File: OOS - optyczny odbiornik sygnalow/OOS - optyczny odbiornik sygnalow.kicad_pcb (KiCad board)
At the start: 2 copper layers, 72 x 79.5 mm, 124 parts, among them J1 Conn_01x02_Pin, J4 Conn_01x02_Socket, J5 Conn_Coaxial, J6 USB_C_Receptacle, Q1 SI2301CDS-T1-GE3, Q2 AOSS32334C, Q3 AOSS32334C, SW1 SW_Rotary_1x8_MP, U1 OPA300AIDBVR, U2 OPA300AIDBVR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

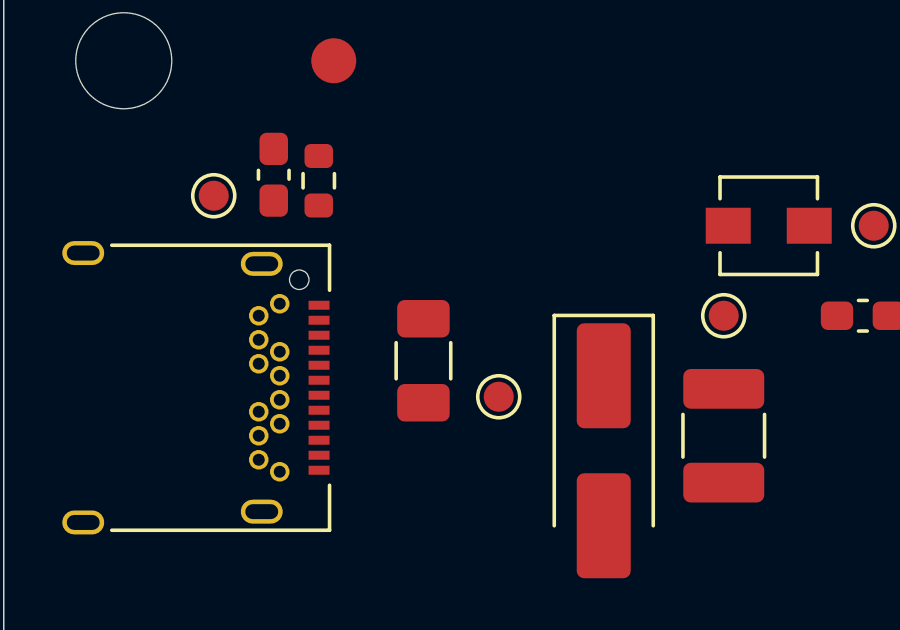
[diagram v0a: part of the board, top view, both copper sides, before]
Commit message: Move testpoint TP37
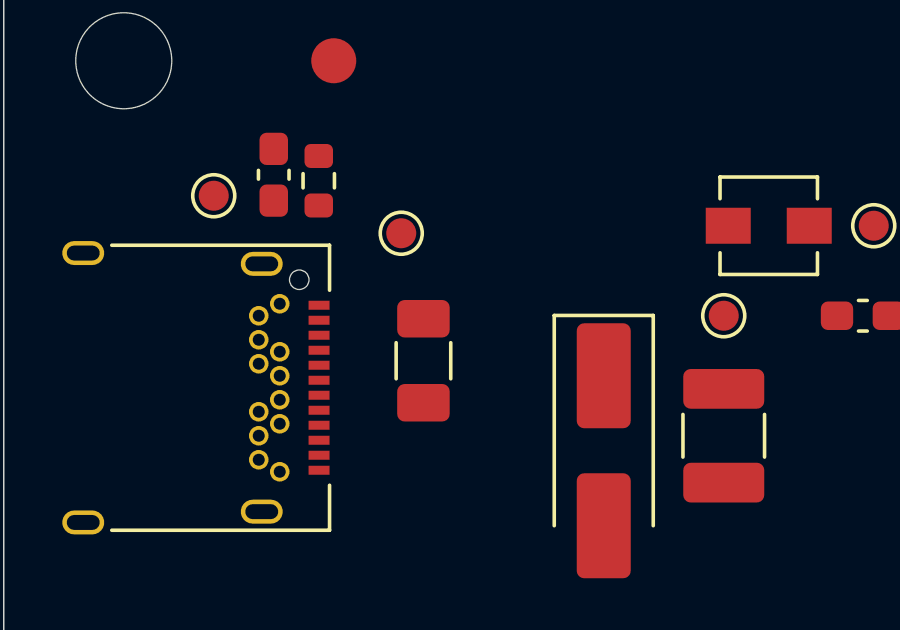
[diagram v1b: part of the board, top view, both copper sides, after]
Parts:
- moved TP37 6.35 mm to (211.7, 38.1)
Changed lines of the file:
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@@
 	(footprint "TestPoint:TestPoint_Pad_D1.0mm"
 		(layer "F.Cu")
-		(at 214.92 43.58 180)
+		(at 211.67 38.13 180)
 		(descr "SMD pad as test Point, diameter 1.0mm")
 		(tags "test point SMD pad")

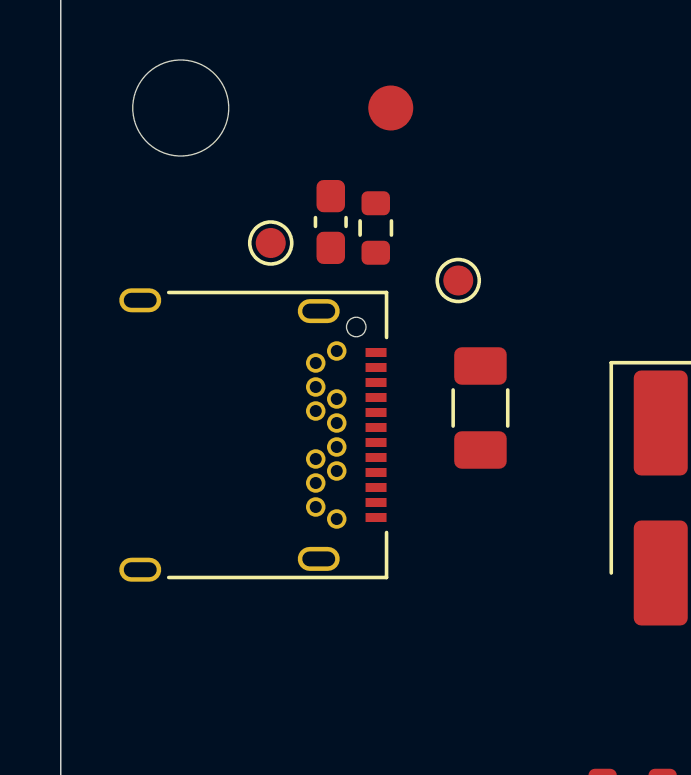
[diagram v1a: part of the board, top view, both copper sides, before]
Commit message: Added polygon for USB3.2, move TP37 on a schematic
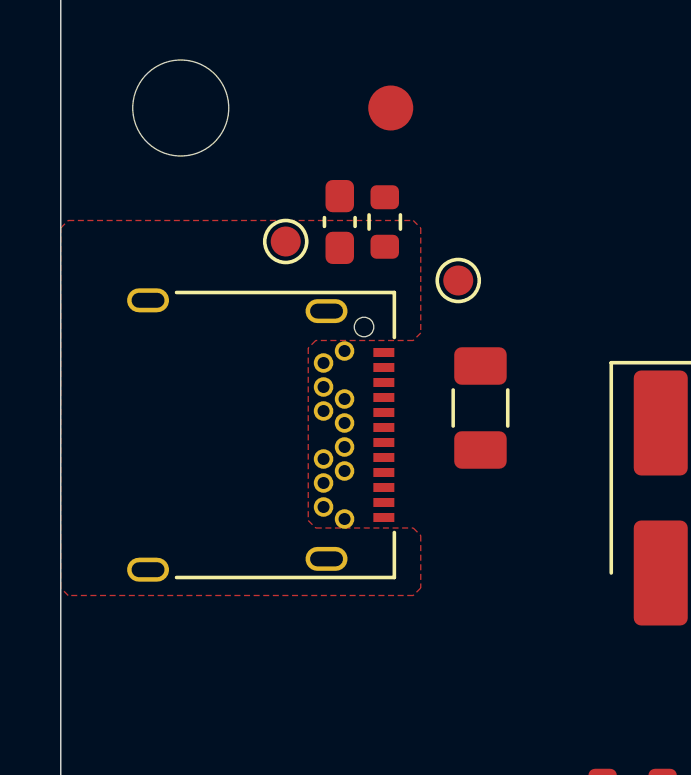
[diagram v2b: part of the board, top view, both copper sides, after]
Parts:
- moved TP38 0.50 mm to (205.9, 36.8)
- moved R26 0.36 mm to (209.2, 36.2)
- moved C25 0.30 mm to (207.7, 36.2)
- moved J6 0.26 mm to (204.2, 43.3)
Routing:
- added copper zone on F.Cu, net Net-(J6-SHIELD)
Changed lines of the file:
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@@
 	(footprint "Connector_USB:USB_C_Receptacle_Amphenol_12401548E4-2A"
 		(layer "F.Cu")
-		(at 203.91 43.28 -90)
+		(at 204.17 43.28 -90)
 		(descr "USB TYPE C, RA RCPT PCB, Hybrid, https://www.amphenolcanada.com/StockAvailabilityPrice.aspx?From=&PartNum=12401548E4%7e2A")
 		(tags "USB C Type-C Receptacle Hybrid")
@@
 	(footprint "Resistor_SMD:R_0603_1608Metric"
 		(layer "F.Cu")
-		(at 208.92 36.38 90)
+		(at 209.22 36.18 90)
 		(descr "Resistor SMD 0603 (1608 Metric), square (rectangular) end terminal, IPC-7351 nominal, (Body size source: IPC-SM-782 page 72, https://www.pcb-3d.com/wordpress/wp-content/uploads/ipc-sm-782a_amendment_1_and_2.pdf), generated with kicad-footprint-generator")
 		(tags "resistor")
@@
 	(footprint "Capacitor_SMD:C_0603_1608Metric_Pad1.08x0.95mm_HandSolder"
 		(layer "F.Cu")
-		(at 207.42 36.18 90)
+		(at 207.72 36.18 90)
 		(descr "Capacitor SMD 0603 (1608 Metric), square (rectangular) end terminal, IPC-7351 nominal with elongated pad for handsoldering. (Body size source: IPC-SM-782 page 76, https://www.pcb-3d.com/wordpress/wp-content/uploads/ipc-sm-782a_amendment_1_and_2.pdf), generated with kicad-footprint-generator")
 		(tags "capacitor handsolder")
@@
 	(footprint "TestPoint:TestPoint_Pad_D1.0mm"
 		(layer "F.Cu")
-		(at 205.42 36.88)
+		(at 205.92 36.83)
 		(descr "SMD pad as test Point, diameter 1.0mm")
 		(tags "test point SMD pad")
@@
 		(net 56)
 	)
+	(zone
+		(net 19)
+		(net_name "Net-(J6-SHIELD)")
+		(layer "F.Cu")
+		(name "Shield")
+		(hatch edge 0.5)
+		(connect_pads
+			(clearance 0.5)
+		)
+		(min_thickness 0.25)
+		(filled_areas_thickness no)
+		(fill yes
+			(thermal_gap 0.2)
+			(thermal_bridge_width 0.4)
+		)
+		(polygon
+			(pts
+				(xy 210.17 36.13) (xy 210.42 36.38) (xy 210.42 39.88) (xy 210.17 40.13) (xy 206.92 40.13) (xy 206.67 40.38)
+				(xy 206.67 46.13) (xy 206.92 46.38) (xy 210.17 46.38) (xy 210.42 46.63) (xy 210.42 48.38) (xy 210.17 48.63)
+				(xy 198.67 48.63) (xy 198.42 48.38) (xy 198.42 36.38) (xy 198.67 36.13)
+			)
+		)
+	)
 	(embedded_fonts no)

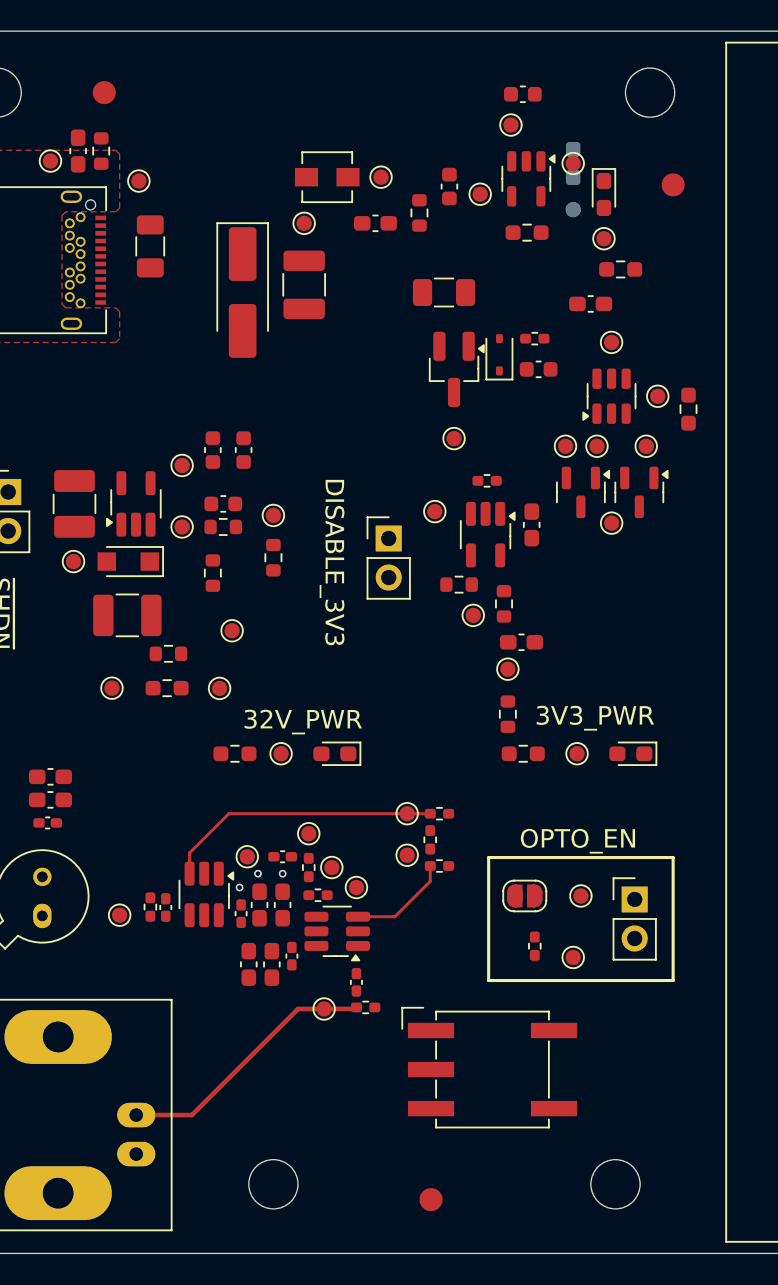
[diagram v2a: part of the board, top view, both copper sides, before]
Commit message: Moved TP37 on schematic, Added LED diode with resistor for +5V indication, improved component placement for USB3.2
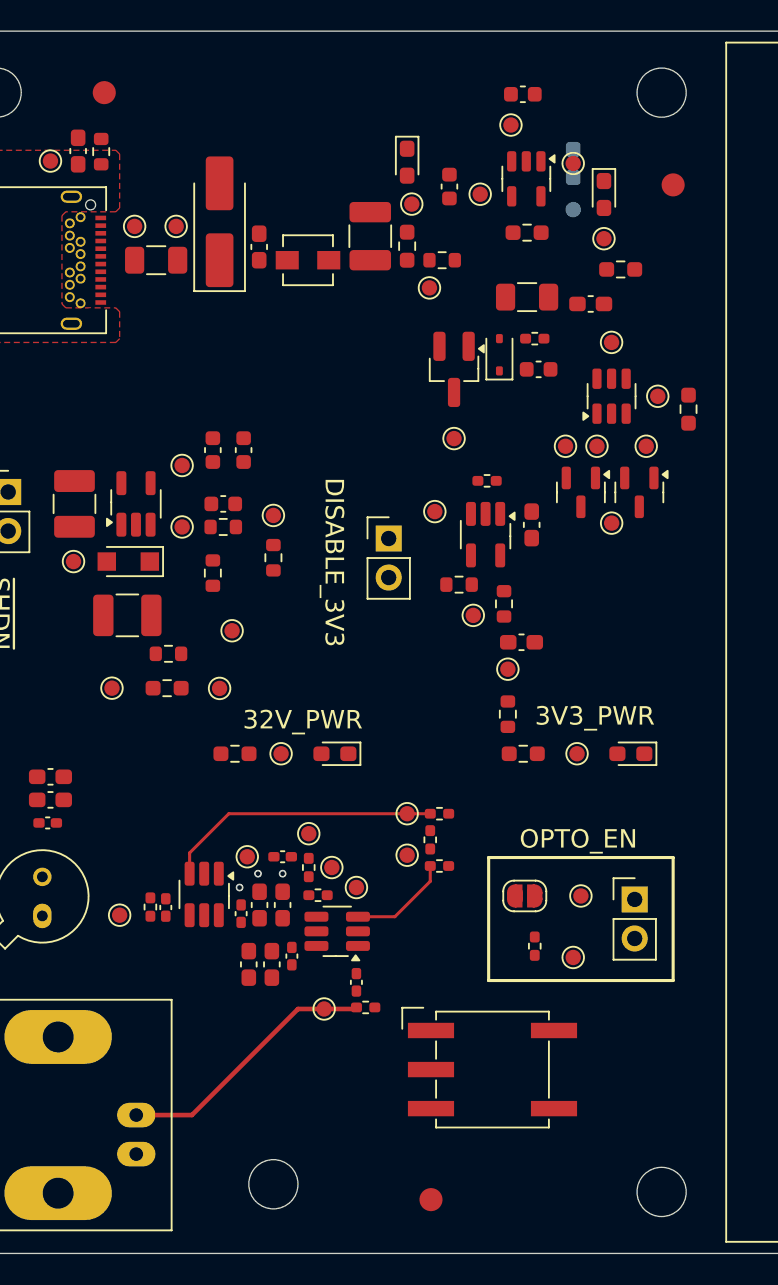
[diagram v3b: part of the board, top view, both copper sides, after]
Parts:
- added D8: LED, Diode_SMD:D_0603_1608Metric_Pad1.05x0.95mm_HandSolder, F.Cu at (229.1, 36.9)
- added R27: 2k2, Resistor_SMD:R_0603_1608Metric_Pad0.98x0.95mm_HandSolder, F.Cu at (229.1, 42.4)
- added TP39: TestPoint_Small, TestPoint:TestPoint_Pad_D1.0mm, F.Cu at (229.4, 39.6)
- moved TP35 8.33 mm to (214.1, 41.1)
- moved TP36 7.86 mm to (230.6, 45.1)
- moved C24 7.72 mm to (219.5, 42.4), turned to 90 degrees
- moved L2 5.54 mm to (222.7, 43.3)
- moved F2 5.41 mm to (236.9, 45.7)
- moved C23 5.34 mm to (226.7, 41.7), turned to 90 degrees
- moved D7 4.84 mm to (216.9, 40.8), turned to 90 degrees
- moved R25 3.41 mm to (231.4, 43.3), turned to 180 degrees
- moved H4 3.04 mm to (245.7, 103.9)
- moved TP37 2.96 mm to (211.4, 41.1)
- moved F1 0.98 mm to (212.8, 43.3), turned to 0 degrees
- moved H2 0.75 mm to (245.7, 32.4)
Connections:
- C23 pad 1: /Sekcja_USB/C24_net -> +5V
- C24 pad 1: +5V -> /Sekcja_USB/C24_net
- R1 pad 1: +32V -> Net-(D4-K)
- R2 pad 1: +3V3 -> Net-(U6-V_{OUT})
- TP37 pad 1: /Sekcja_USB/C24_net -> /Sekcja_USB/J6_Vbus

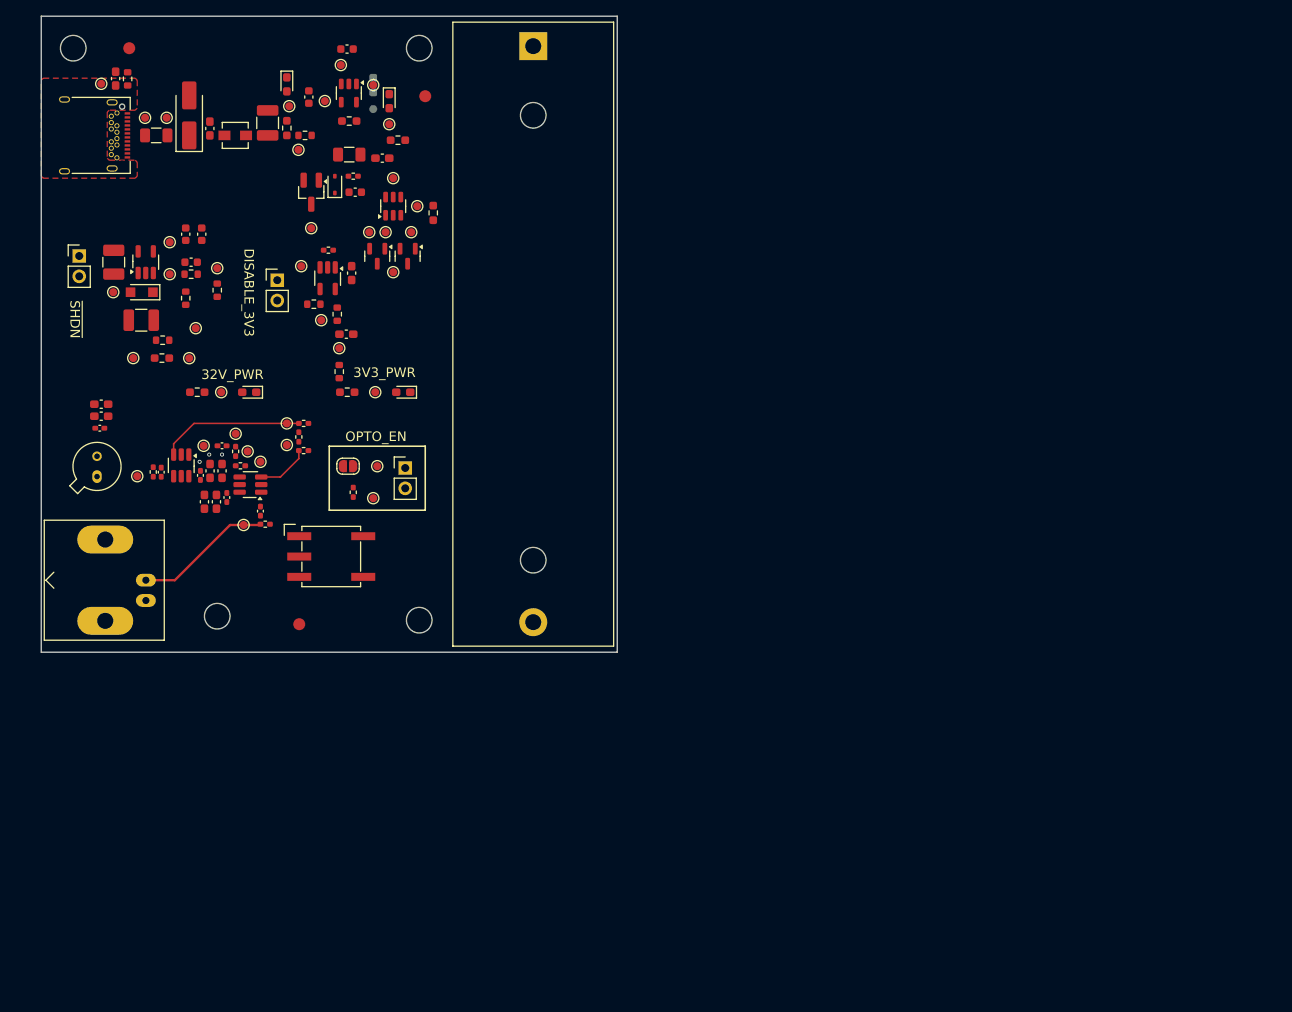
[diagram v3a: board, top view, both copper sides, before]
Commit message: trying a different placement for components
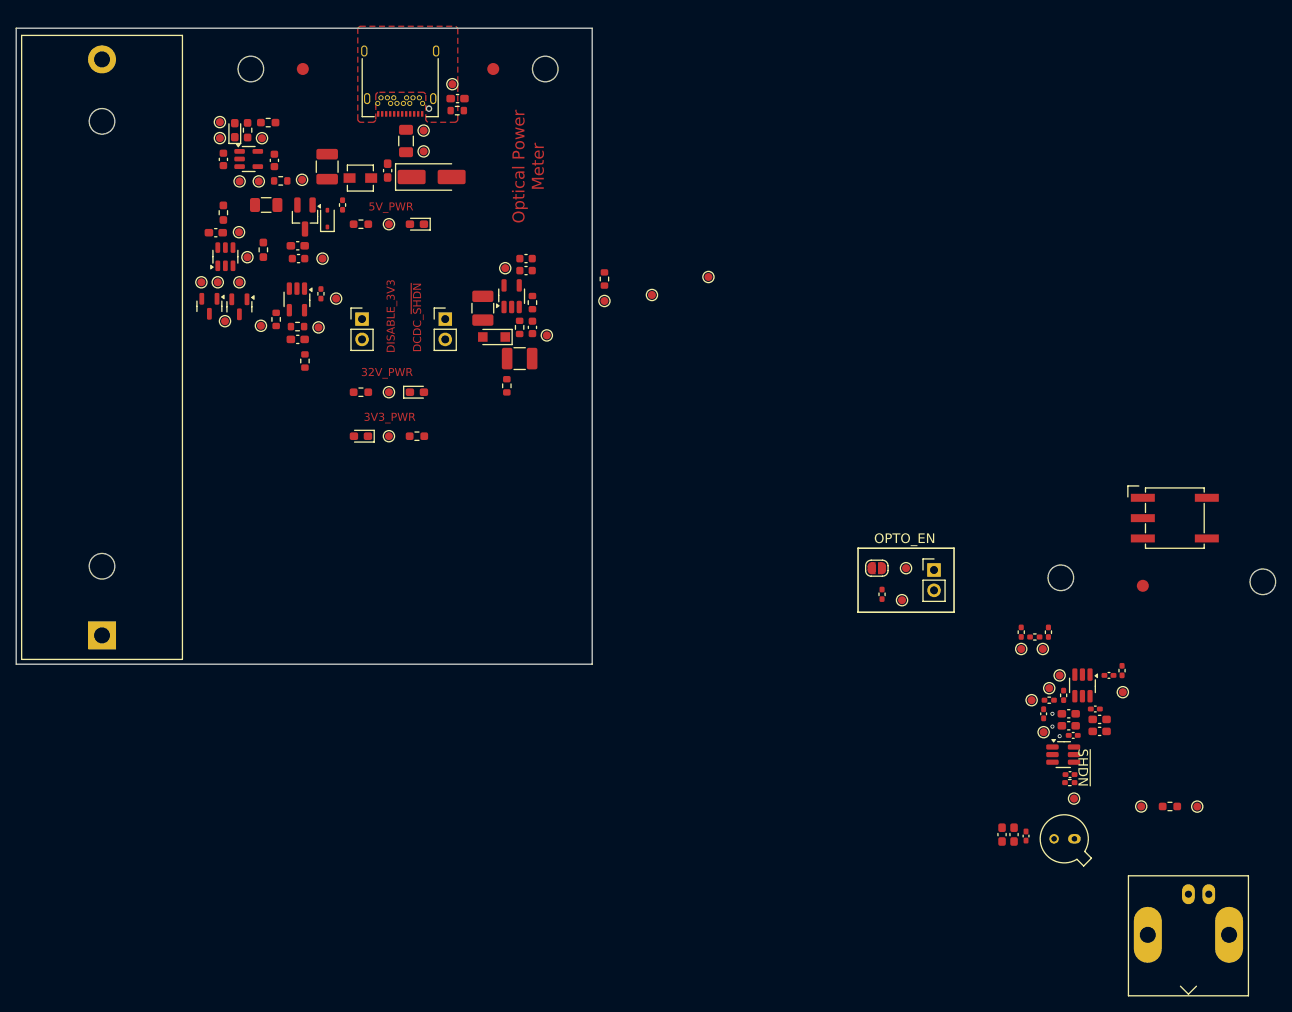
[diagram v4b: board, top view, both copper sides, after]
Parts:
- R20, TP22: moved to F.Cu
- moved R3 137.9 mm to (339.5, 127.2)
- moved TP1 137.9 mm to (342.9, 127.2)
- moved TP2 137.9 mm to (335.9, 127.2)
- moved J5 136.1 mm to (341.8, 138.1), turned to 180 degrees
- moved D3 130.3 mm to (327.6, 131.2), turned to 180 degrees
- moved C9 126.5 mm to (321.5, 130.9), turned to 90 degrees
- moved C8 125.5 mm to (320.0, 130.7), turned to 90 degrees
- moved C7 124.8 mm to (318.5, 130.7), turned to -90 degrees
- moved TP6 123.8 mm to (327.5, 126.2), turned to 180 degrees
- moved R8 121.0 mm to (327.0, 124.2), turned to 180 degrees
- moved C10 119.7 mm to (327.0, 123.2), turned to 180 degrees
- moved U1 116.0 mm to (326.2, 120.7), turned to 0 degrees
- moved C2 115.5 mm to (330.7, 117.8), turned to 0 degrees
- moved C5 113.8 mm to (327.4, 118.3), turned to 180 degrees
- moved C4 113.7 mm to (330.7, 116.3), turned to 0 degrees
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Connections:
- D1 pad 1: 0V -> Net-(D1-K)
- D1 pad 2: Net-(D1-A) -> +32V
- D2 pad 1: 0V -> Net-(D2-K)
- D2 pad 2: Net-(D2-A) -> +3V3
- R1 pad 1: Net-(D4-K) -> Net-(D1-K)
- R1 pad 2: Net-(D1-A) -> 0V
- R2 pad 1: Net-(U6-V_{OUT}) -> Net-(D2-K)
- R2 pad 2: Net-(D2-A) -> 0V
- TP17 pad 1: Net-(D1-A) -> Net-(D1-K)
- TP33 pad 1: Net-(D2-A) -> Net-(D2-K)
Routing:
- net /Sekcja_Analogowa/U1_TIA_+: track 18.1 -> 0.00 mm
- net /Sekcja_Analogowa/U2_x10_Out_AC: track 17.2 -> 0.00 mm
- net /Sekcja_Analogowa/U2_x10_+: track 6.65 -> 0.00 mm
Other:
- board text added: "5V_PWR"
- board text added: "DCDC_~{SHDN}"
- board text added: "Optical Power Meter"
